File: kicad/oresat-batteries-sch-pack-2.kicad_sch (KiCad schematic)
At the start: 85 parts, among them Q11 SI7111EDN-T1-GE3, Q22 SQS484ENW-T1_GE3, Q24 PM45VEN, Q25 PM45VEN, Q26 PM45VEN, Q27 PM45VEN, Q30 SI7111EDN-T1-GE3, Q31 SI7111EDN-T1-GE3, Q32 NTR4101, Q33 NTR4101, Q34 SI7111EDN-T1-GE3, Q35 SI7111EDN-T1-GE3, Q36 SI7111EDN-T1-GE3, Q37 SI7111EDN-T1-GE3, U13 S-8209AAA-T8T1U, U14 S-8209AAA-T8T1U, U15 LTC4412, U16 LTC4412, U17 MAX17205G

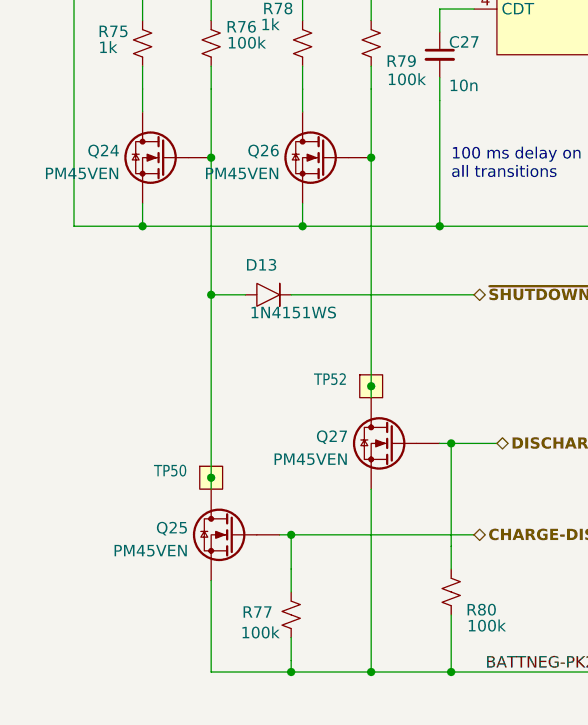
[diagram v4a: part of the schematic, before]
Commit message: Progress on battery card v4
Moved in -batt cutoffs, which caused a lot of pain and suffering. Started updating BOM, and fixed all transistor packages. Updated resistor packages, too. Still needs a lot of cleanup, but probably 80% done now.
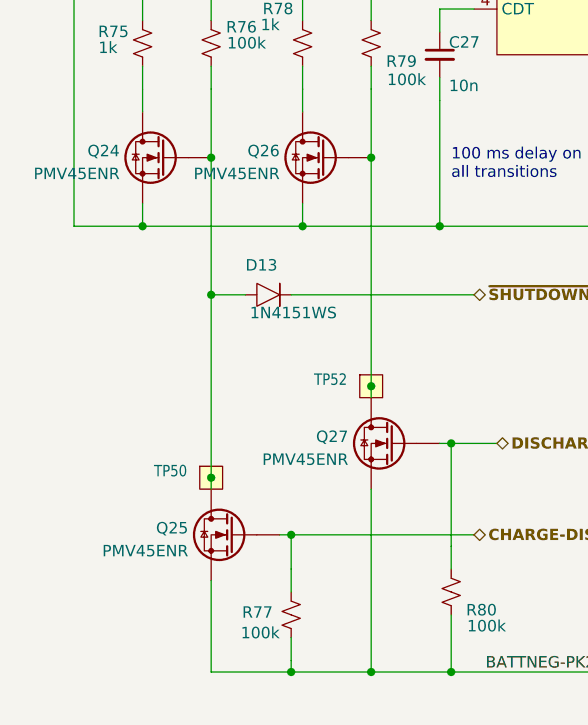
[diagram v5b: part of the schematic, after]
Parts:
- C11: footprint oresat-passives:0805-B-NOSILK -> oresat-passives:0805-C-NOSILK
- C26, C27, C28, C29, C30, C31, C32, C33, C34, C35, C36: footprint oresat-passives:c_0603-SMALL -> oresat-passives:0603-C-NOSILK
- Q11, Q30, Q31, Q34, Q35, Q36, Q37: DIS Digi-Key -> DigiKey
- Q22: DIS (none) -> DigiKey
- Q24, Q25, Q26, Q27: value PM45VEN -> PMV45ENR; footprint oresat-batteries:SOT23-3 -> Package_TO_SOT_SMD:SOT-23; DIS Digi-Key -> DigiKey
- Q32, Q33: footprint oresat-batteries:SOT23-3 -> Package_TO_SOT_SMD:SOT-23; DIS Digi-Key -> DigiKey
- R101: footprint oresat-batteries:.0603-C-NOSILK -> oresat-passives:0603-C-NOSILK; DISTRIBUTOR Digi-key -> (none)
- R103, R56, R70, R75, R76, R77, R78, R79, R80, R81, R82, R83, R84, R86, R88, R89, R90, R91, R94, R97: footprint oresat-batteries:.0603-C-NOSILK -> oresat-passives:0603-C-NOSILK
- R92: footprint oresat-batteries:1206-C -> oresat-passives:1206-C
- R95, R96: footprint oresat-batteries:.0603-C-NOSILK -> oresat-passives:0603-C-NOSILK; DIS Digi-Key -> DigiKey
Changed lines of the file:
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@@
 			)
 		)
-		(property "Footprint" "oresat-batteries:.0603-C-NOSILK"
+		(property "Footprint" "oresat-passives:0603-C-NOSILK"
 			(at 265.43 36.83 0)
 			(effects
@@
 			)
 		)
-		(property "Footprint" "oresat-batteries:.0603-C-NOSILK"
+		(property "Footprint" "oresat-passives:0603-C-NOSILK"
 			(at 250.19 191.77 0)
 			(effects
@@
 			)
 		)
-		(property "Footprint" "oresat-batteries:.0603-C-NOSILK"
+		(property "Footprint" "oresat-passives:0603-C-NOSILK"
 			(at 233.68 82.55 0)
 			(effects
@@
 			)
 		)
+		(property "DIS" "DigiKey"
+			(at 256.54 217.17 0)
+			(effects
+				(font
+					(size 1.27 1.27)
+				)
+				(hide yes)
+			)
+		)
 		(pin "2"
 		)
@@
 			)
 		)
-		(property "Footprint" "oresat-passives:0805-B-NOSILK"
+		(property "Footprint" "oresat-passives:0805-C-NOSILK"
 			(at 259.08 62.23 0)
 			(effects
@@
 			)
 		)
-		(property "Footprint" "oresat-batteries:.0603-C-NOSILK"
+		(property "Footprint" "oresat-passives:0603-C-NOSILK"
 			(at 265.43 217.17 0)
 			(effects
@@
 			)
 		)
-		(property "Value" "PM45VEN"
+		(property "Value" "PMV45ENR"
 			(at 55.88 195.58 0)
 			(effects
@@
 			)
 		)
-		(property "Footprint" "oresat-batteries:SOT23-3"
+		(property "Footprint" "Package_TO_SOT_SMD:SOT-23"
 			(at 55.88 190.5 0)
 			(effects
@@
 			)
 		)
-		(property "DIS" "Digi-Key"
+		(property "DIS" "DigiKey"
 			(at 60.96 193.04 0)
 			(effects
@@
 			)
 		)
-		(property "Footprint" "oresat-batteries:.0603-C-NOSILK"
+		(property "Footprint" "oresat-passives:0603-C-NOSILK"
 			(at 151.13 109.22 0)
 			(effects
@@
 			)
 		)
-		(property "Footprint" "oresat-batteries:.0603-C-NOSILK"
+		(property "Footprint" "oresat-passives:0603-C-NOSILK"
 			(at 48.26 180.34 0)
 			(effects
@@
 			)
 		)
-		(property "Footprint" "oresat-batteries:SOT23-3"
+		(property "Footprint" "Package_TO_SOT_SMD:SOT-23"
 			(at 252.73 144.78 0)
 			(effects
@@
 			)
 		)
-		(property "DIS" "Digi-Key"
+		(property "DIS" "DigiKey"
 			(at 247.65 142.24 0)
 			(effects
@@
 			)
 		)
-		(property "Footprint" "oresat-batteries:.0603-C-NOSILK"
+		(property "Footprint" "oresat-passives:0603-C-NOSILK"
 			(at 285.75 71.12 0)
 			(effects
@@
 			)
 		)
-		(property "Footprint" "oresat-batteries:.0603-C-NOSILK"
+		(property "Footprint" "oresat-passives:0603-C-NOSILK"
 			(at 243.84 137.16 0)
 			(effects
@@
 			)
 		)
-		(property "Footprint" "oresat-batteries:SOT23-3"
+		(property "Footprint" "Package_TO_SOT_SMD:SOT-23"
 			(at 252.73 179.07 0)
 			(effects
@@
 			)
 		)
-		(property "DIS" "Digi-Key"
+		(property "DIS" "DigiKey"
 			(at 247.65 176.53 0)
 			(effects
@@
 			)
 		)
-		(property "Footprint" "oresat-passives:c_0603-SMALL"
+		(property "Footprint" "oresat-passives:0603-C-NOSILK"
 			(at 317.5 57.15 0)
 			(effects
@@
 			)
 		)
-		(property "Footprint" "oresat-passives:c_0603-SMALL"
+		(property "Footprint" "oresat-passives:0603-C-NOSILK"
 			(at 307.34 180.34 0)
 			(effects
@@
 			)
 		)
-		(property "Value" "PM45VEN"
+		(property "Value" "PMV45ENR"
 			(at 45.72 237.49 0)
 			(effects
@@
 			)
 		)
-		(property "Footprint" "oresat-batteries:SOT23-3"
+		(property "Footprint" "Package_TO_SOT_SMD:SOT-23"
 			(at 45.72 232.41 0)
 			(effects
@@
 			)
 		)
-		(property "DIS" "Digi-Key"
+		(property "DIS" "DigiKey"
 			(at 50.8 234.95 0)
 			(effects
@@
 			)
 		)
-		(property "Footprint" "oresat-passives:c_0603-SMALL"
+		(property "Footprint" "oresat-passives:0603-C-NOSILK"
 			(at 313.69 133.35 0)
 			(effects
@@
 			)
 		)
-		(property "Footprint" "oresat-batteries:.0603-C-NOSILK"
+		(property "Footprint" "oresat-passives:0603-C-NOSILK"
 			(at 243.84 171.45 0)
 			(effects
@@
 			)
 		)
-		(property "Footprint" "oresat-batteries:.0603-C-NOSILK"
+		(property "Footprint" "oresat-passives:0603-C-NOSILK"
 			(at 57.15 243.84 0)
 			(effects
@@
 			)
 		)
-		(property "Footprint" "oresat-batteries:.0603-C-NOSILK"
+		(property "Footprint" "oresat-passives:0603-C-NOSILK"
 			(at 74.93 241.3 0)
 			(effects
@@
 			)
 		)
-		(property "DIS" "Digi-Key"
+		(property "DIS" "DigiKey"
 			(at 280.67 52.07 0)
 			(effects
@@
 			)
 		)
-		(property "Footprint" "oresat-passives:c_0603-SMALL"
+		(property "Footprint" "oresat-passives:0603-C-NOSILK"
 			(at 369.57 129.54 0)
 			(effects
@@
 			)
 		)
-		(property "Footprint" "oresat-batteries:.0603-C-NOSILK"
+		(property "Footprint" "oresat-passives:0603-C-NOSILK"
 			(at 115.57 171.45 0)
 			(effects
@@
 			)
 		)
-		(property "Footprint" "oresat-passives:c_0603-SMALL"
+		(property "Footprint" "oresat-passives:0603-C-NOSILK"
 			(at 359.41 129.54 0)
 			(effects
@@
 			)
 		)
-		(property "Footprint" "oresat-passives:c_0603-SMALL"
+		(property "Footprint" "oresat-passives:0603-C-NOSILK"
 			(at 198.12 50.8 0)
 			(effects
@@
 			)
 		)
-		(property "DIS" "Digi-Key"
+		(property "DIS" "DigiKey"
 			(at 237.49 52.07 0)
 			(effects
@@
 			)
 		)
-		(property "DIS" "Digi-Key"
+		(property "DIS" "DigiKey"
 			(at 237.49 76.2 0)
 			(effects
@@
 			)
 		)
-		(property "Footprint" "oresat-passives:c_0603-SMALL"
+		(property "Footprint" "oresat-passives:0603-C-NOSILK"
 			(at 132.08 138.43 0)
 			(effects
@@
 			)
 		)
-		(property "Footprint" "oresat-batteries:.0603-C-NOSILK"
+		(property "Footprint" "oresat-passives:0603-C-NOSILK"
 			(at 92.71 152.4 0)
 			(effects
@@
 			)
 		)
-		(property "Footprint" "oresat-batteries:.0603-C-NOSILK"
+		(property "Footprint" "oresat-passives:0603-C-NOSILK"
 			(at 250.19 157.48 0)
 			(effects
@@
 			)
 		)
-		(property "DIS" "Digi-Key"
+		(property "DIS" "DigiKey"
 			(at 256.54 148.59 0)
 			(effects
@@
 			)
 		)
-		(property "Footprint" "oresat-batteries:.0603-C-NOSILK"
+		(property "Footprint" "oresat-passives:0603-C-NOSILK"
 			(at 40.64 180.34 0)
 			(effects
@@
 			)
 		)
-		(property "DIS" "Digi-Key"
+		(property "DIS" "DigiKey"
 			(at 256.54 182.88 0)
 			(effects
@@
 			)
 		)
-		(property "Footprint" "oresat-passives:c_0603-SMALL"
+		(property "Footprint" "oresat-passives:0603-C-NOSILK"
 			(at 307.34 154.94 0)
 			(effects
@@
 			)
 		)
-		(property "Footprint" "oresat-batteries:.0603-C-NOSILK"
+		(property "Footprint" "oresat-passives:0603-C-NOSILK"
 			(at 58.42 180.34 0)
 			(effects
@@
 			)
 		)
-		(property "Footprint" "oresat-batteries:.0603-C-NOSILK"
+		(property "Footprint" "oresat-passives:0603-C-NOSILK"
 			(at 297.18 168.91 0)
 			(effects
@@
 			)
 		)
-		(property "DIS" "Digi-Key"
+		(property "DIS" "DigiKey"
 			(at 297.18 168.91 0)
 			(effects
@@
 			)
 		)
-		(property "Footprint" "oresat-batteries:1206-C"
+		(property "Footprint" "oresat-passives:1206-C"
 			(at 259.08 236.22 0)
 			(effects
@@
 			)
 		)
-		(property "Value" "PM45VEN"
+		(property "Value" "PMV45ENR"
 			(at 38.1 195.58 0)
 			(effects
@@
 			)
 		)
-		(property "Footprint" "oresat-batteries:SOT23-3"
+		(property "Footprint" "Package_TO_SOT_SMD:SOT-23"
 			(at 38.1 190.5 0)
 			(effects
@@
 			)
 		)
-		(property "DIS" "Digi-Key"
+		(property "DIS" "DigiKey"
 			(at 43.18 193.04 0)
 			(effects
@@
 			)
 		)
-		(property "Footprint" "oresat-passives:c_0603-SMALL"
+		(property "Footprint" "oresat-passives:0603-C-NOSILK"
 			(at 33.02 170.18 0)
 			(effects
@@
 			)
 		)
-		(property "DIS" "Digi-Key"
+		(property "DIS" "DigiKey"
 			(at 261.62 30.48 0)
 			(effects
@@
 			)
 		)
-		(property "Footprint" "oresat-batteries:.0603-C-NOSILK"
+		(property "Footprint" "oresat-passives:0603-C-NOSILK"
 			(at 66.04 180.34 0)
 			(effects
@@
 			)
 		)
-		(property "Footprint" "oresat-batteries:.0603-C-NOSILK"
+		(property "Footprint" "oresat-passives:0603-C-NOSILK"
 			(at 387.35 167.64 0)
 			(effects
@@
 			)
 		)
-		(property "Footprint" "oresat-passives:c_0603-SMALL"
+		(property "Footprint" "oresat-passives:0603-C-NOSILK"
 			(at 73.66 181.61 0)
 			(effects
@@
 			)
 		)
-		(property "Footprint" "oresat-passives:c_0603-SMALL"
+		(property "Footprint" "oresat-passives:0603-C-NOSILK"
 			(at 115.57 127 0)
 			(effects
@@
 			)
 		)
-		(property "DIS" "Digi-Key"
+		(property "DIS" "DigiKey"
 			(at 280.67 77.47 0)
 			(effects
@@
 			)
 		)
-		(property "Value" "PM45VEN"
+		(property "Value" "PMV45ENR"
 			(at 63.5 227.33 0)
 			(effects
@@
 			)
 		)
-		(property "Footprint" "oresat-batteries:SOT23-3"
+		(property "Footprint" "Package_TO_SOT_SMD:SOT-23"
 			(at 63.5 222.25 0)
 			(effects
@@
 			)
 		)
-		(property "DIS" "Digi-Key"
+		(property "DIS" "DigiKey"
 			(at 68.58 224.79 0)
 			(effects
@@
 			)
 		)
-		(property "Footprint" "oresat-batteries:.0603-C-NOSILK"
+		(property "Footprint" "oresat-passives:0603-C-NOSILK"
 			(at 250.19 222.25 0)
 			(effects
@@
 			)
 		)
-		(property "Footprint" "oresat-batteries:.0603-C-NOSILK"
+		(property "Footprint" "oresat-passives:0603-C-NOSILK"
 			(at 375.92 167.64 0)
 			(effects
@@
 			)
 		)
-		(property "DISTRIBUTOR" "Digi-key"
-			(at 375.92 167.64 0)
-			(effects
-				(font
-					(size 1.27 1.27)
-				)
-				(justify left bottom)
-				(hide yes)
-			)
-		)
 		(property "DPN" "311-10.0KHRCT-ND"
 			(at 375.92 167.64 0)
@@
 			)
 		)
-		(property "Footprint" "oresat-batteries:.0603-C-NOSILK"
+		(property "Footprint" "oresat-passives:0603-C-NOSILK"
 			(at 297.18 128.27 0)
 			(effects
@@
 			)
 		)
-		(property "DIS" "Digi-Key"
+		(property "DIS" "DigiKey"
 			(at 297.18 128.27 0)
 			(effects
@@
 			)
 		)
-		(property "Footprint" "oresat-batteries:.0603-C-NOSILK"
+		(property "Footprint" "oresat-passives:0603-C-NOSILK"
 			(at 115.57 166.37 0)
 			(effects

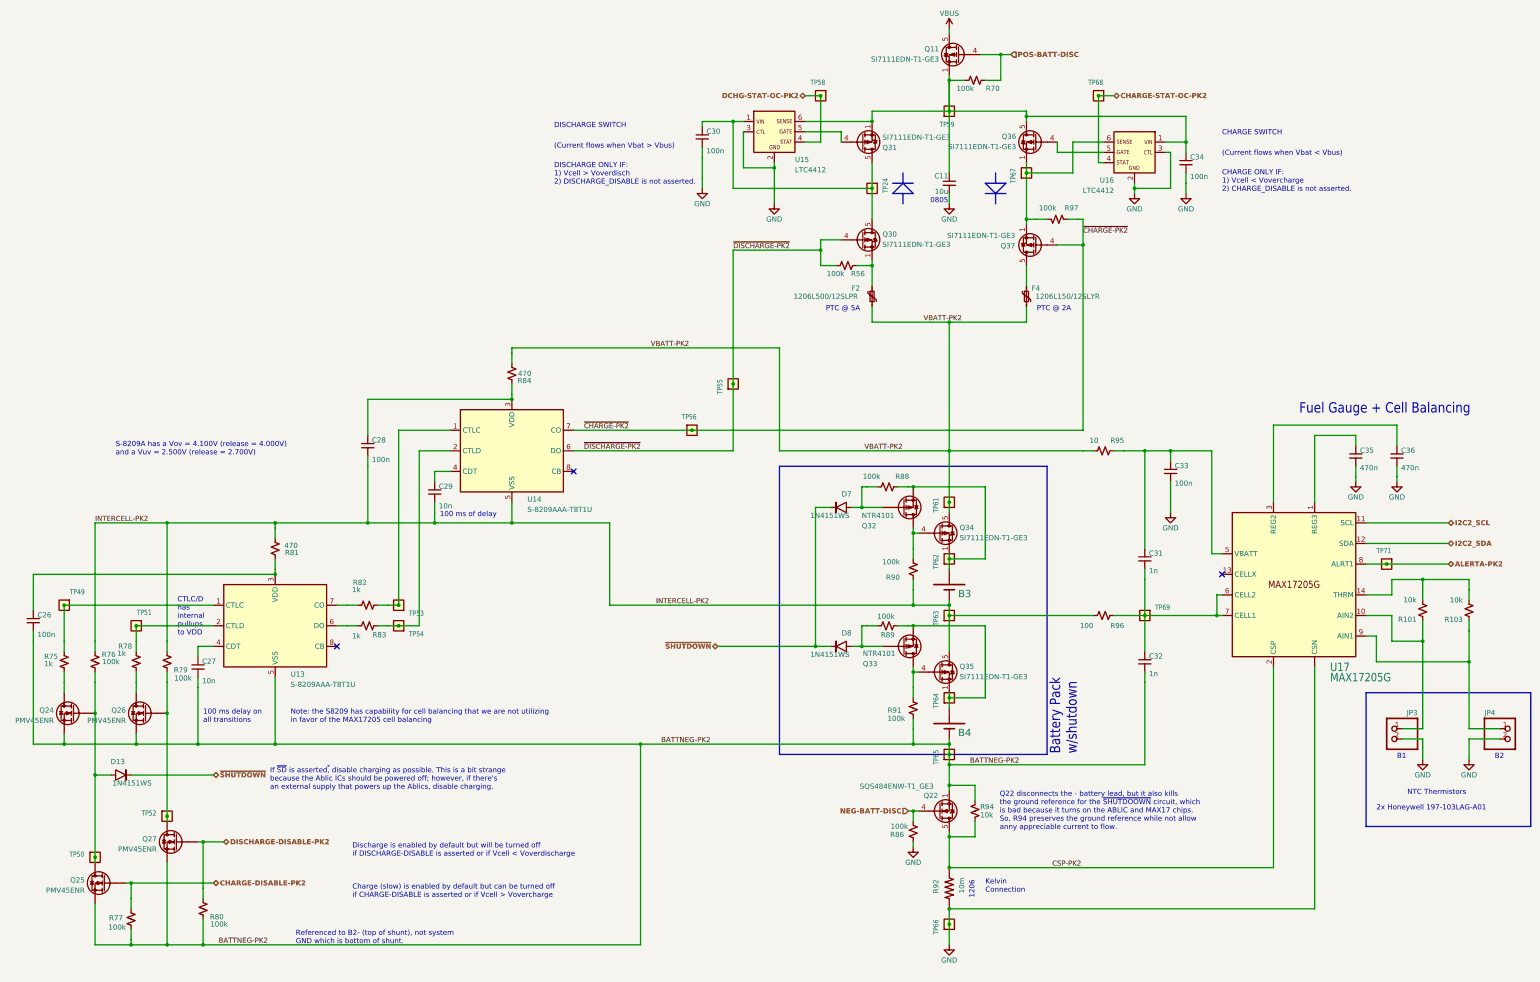
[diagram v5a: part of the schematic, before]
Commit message: Updated BOM, ready for polish and switch to MCXN
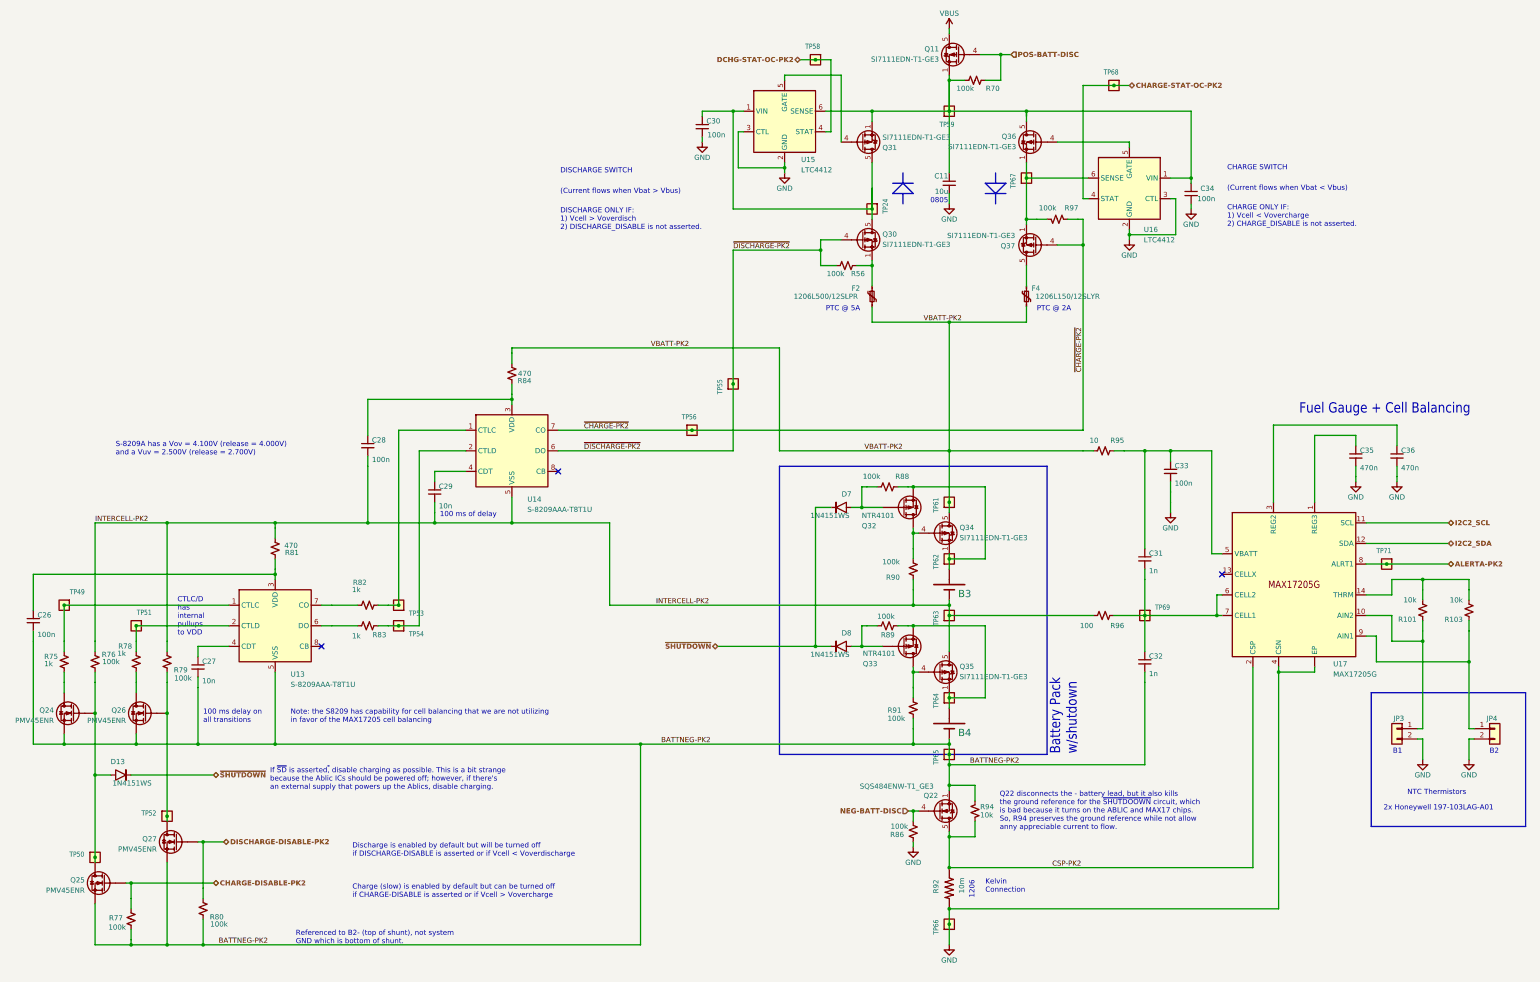
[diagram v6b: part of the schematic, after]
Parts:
- B3, B4: footprint oresat-batteries:18650 -> oresat-misc:18650
- JP3, JP4: footprint oresat-batteries:1X02 -> Connector_PinHeader_2.54mm:PinHeader_1x02_P2.54mm_Vertical; symbol oresat-batteries-eagle-import:PINHD-1X2 -> Connector_Generic:Conn_01x02
- U13, U14: footprint oresat-batteries:TSSOP8 -> Package_SO:TSSOP-8_4.4x3mm_P0.65mm; symbol oresat-batteries-eagle-import:S-8209AXXT -> oresat-ics:S-8209AXXT
- U15, U16: footprint oresat-batteries:SOT23-6 -> Package_TO_SOT_SMD:TSOT-23-6; symbol oresat-batteries-eagle-import:LTC4412 -> Power_Management:LTC4412xS6
- U17: footprint oresat-batteries:21-0137I_T1433-2 -> Package_DFN_QFN:TDFN-14-1EP_3x3mm_P0.4mm_EP1.78x2.35mm_ThermalVias; symbol oresat-batteries-eagle-import:MAX17205G -> oresat-ics:MAX17205G; DIS Digi-Key -> DigiKey; MFR Maxim -> Analog Devices
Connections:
- net GND: now also U17.15 (EP); no longer U17.EP (CSN)
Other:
- moved on the sheet: C30, C34, TP24, TP58, TP67, TP68, U15, U16
